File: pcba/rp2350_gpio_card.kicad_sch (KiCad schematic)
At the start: 38 parts, among them J1 Conn_01x10_Pin, J2 Conn_01x10_Pin, P1 USB_C_Plug_USB2.0, U1 RP2350_60QFN, U2 W25Q128JVS, U4 AP2127K-3.3, Y1 ABM8-272-T3

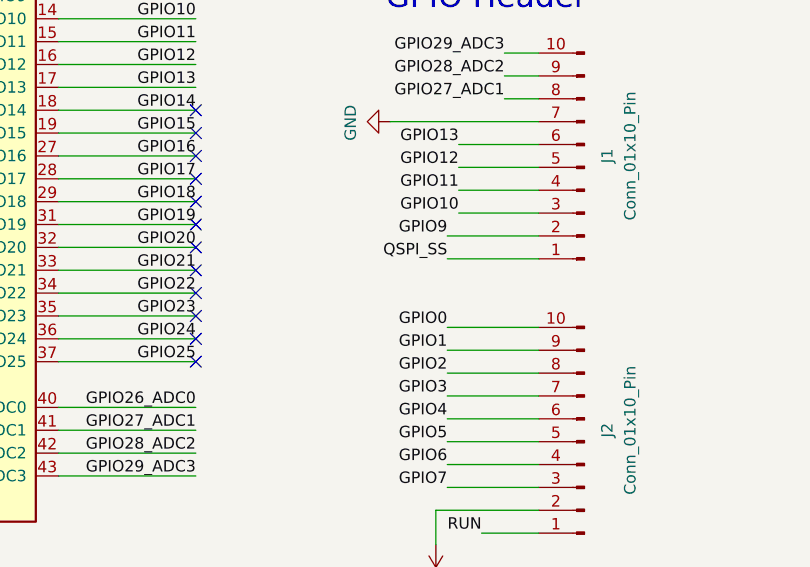
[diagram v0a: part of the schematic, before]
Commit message: small component placement changes
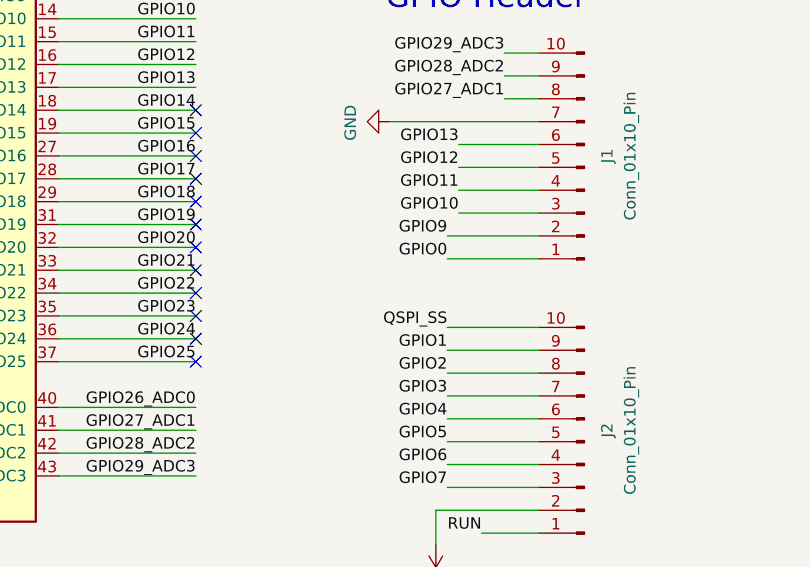
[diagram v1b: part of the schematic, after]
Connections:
- net GPIO0: now also J1.1 (Pin_1); no longer J2.10 (Pin_10)
- net QSPI_SS: now also J2.10 (Pin_10); no longer J1.1 (Pin_1)
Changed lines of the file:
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@@
-		)
-	)
-	(label "GPIO0"
-		(at 175.26 132.08 180)
-		(effects
-			(font
-				(size 1.27 1.27)
-			)
-			(justify right bottom)
 		)
 	)
@@
 		)
 	)
+	(label "QSPI_SS"
+		(at 175.26 132.08 180)
+		(effects
+			(font
+				(size 1.27 1.27)
+			)
+			(justify right bottom)
+		)
+	)
 	(label "QSPI_SD2"
 		(at 254 102.87 0)
@@
 		)
 	)
+	(label "GPIO0"
+		(at 175.26 124.46 180)
+		(effects
+			(font
+				(size 1.27 1.27)
+			)
+			(justify right bottom)
+		)
+	)
 	(label "QSPI_SD0"
 		(at 54.61 87.63 0)
@@
 		(effects
 			(font
-				(size 1.27 1.27)
-			)
-			(justify right bottom)
-		)
-	)
-	(label "QSPI_SS"
-		(at 175.26 124.46 180)
-		(effects
-			(font
